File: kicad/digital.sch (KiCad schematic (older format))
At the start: 15 parts, among them P1 USART0, P3 ISP, P5 hole, P6 hole, P8 hole, P9 hole

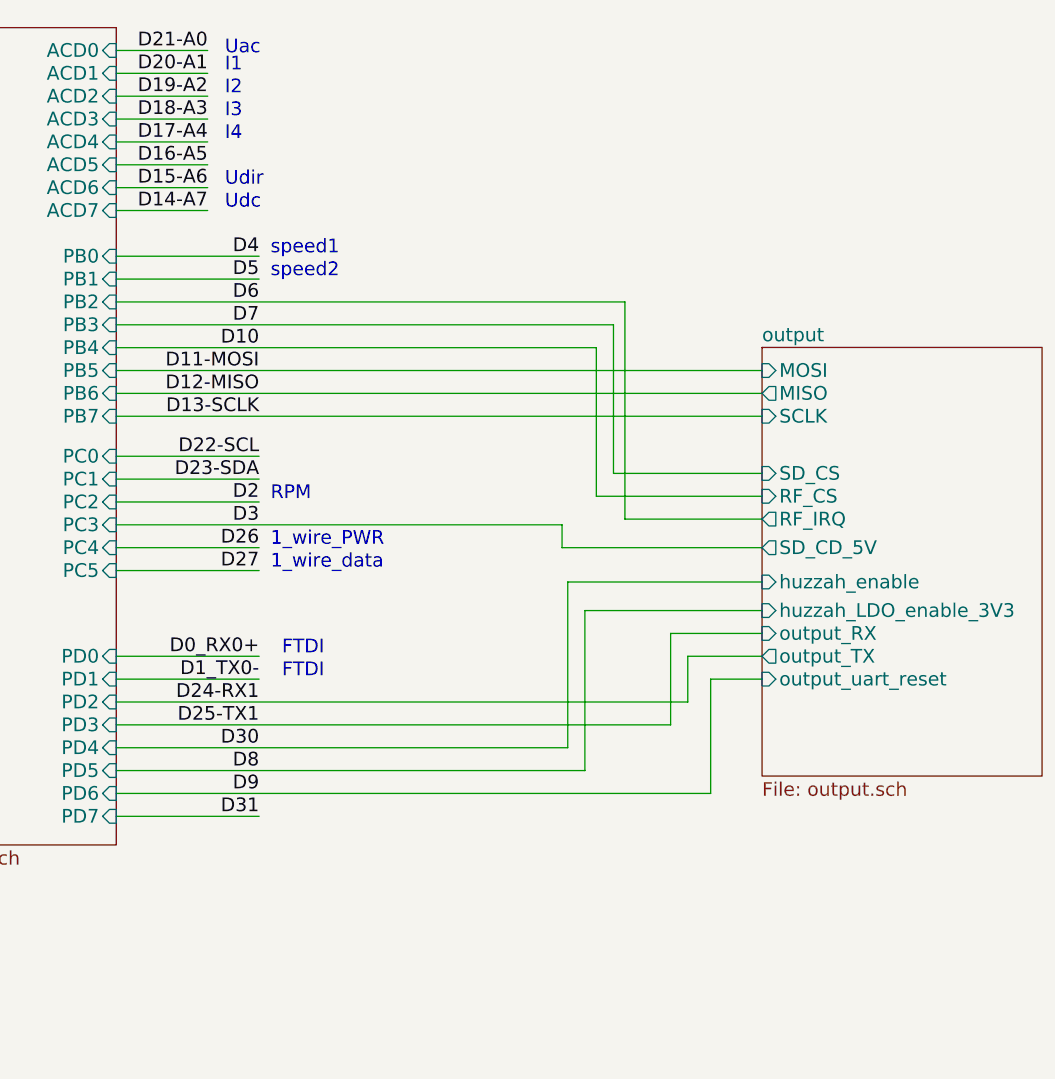
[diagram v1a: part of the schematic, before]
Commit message: add somes notes on schematics
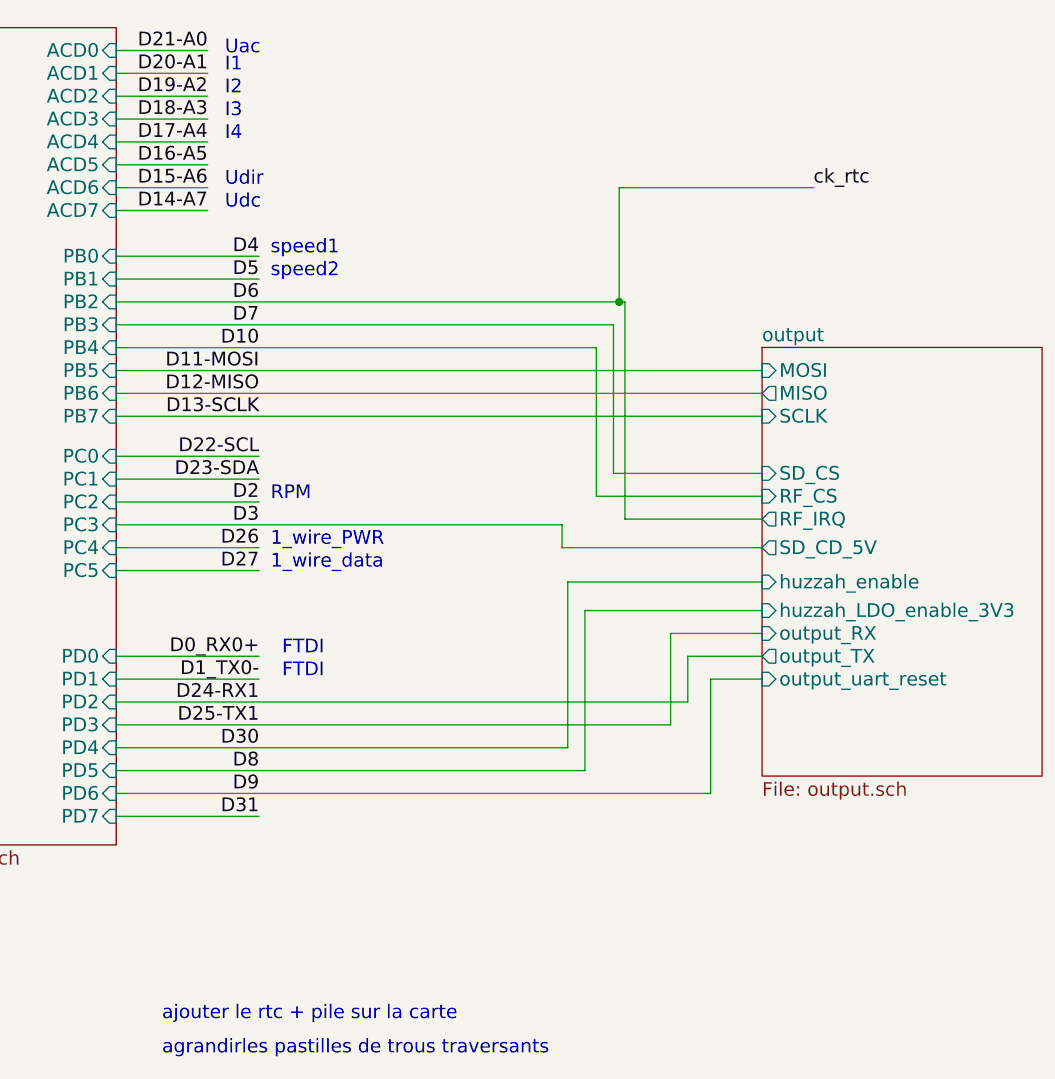
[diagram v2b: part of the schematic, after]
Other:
- note added: "agrandirles pastilles de trous traversants"
- note added: "ajouter le rtc + pile sur la carte"
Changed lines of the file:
@@
 Text Notes 9875 6175 0    60   ~ 0
 +5V\nGND\nTX0\nRX0\nDTR\n3V3
+Text Notes 2850 6400 0    60   ~ 0
+ajouter le rtc + pile sur la carte
+Text Notes 2850 6550 0    60   ~ 0
+agrandirles pastilles de trous traversants
+Wire Wire Line
+	4850 3250 4850 2750
+Wire Wire Line
+	4850 2750 5700 2750
+Connection ~ 4850 3250
+Text Label 5700 2750 0    60   ~ 0
+ck_rtc
 $EndSCHEMATC

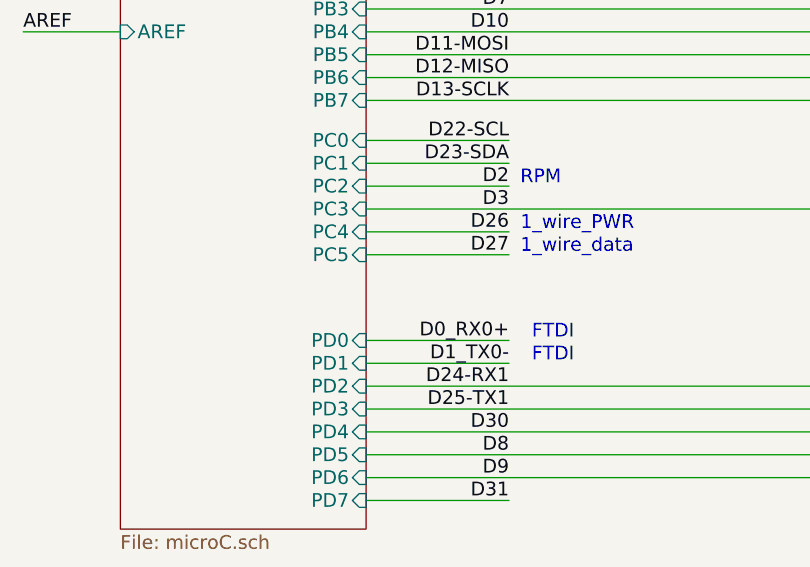
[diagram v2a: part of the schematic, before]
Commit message: Modify micro pins and unify ground in power supply
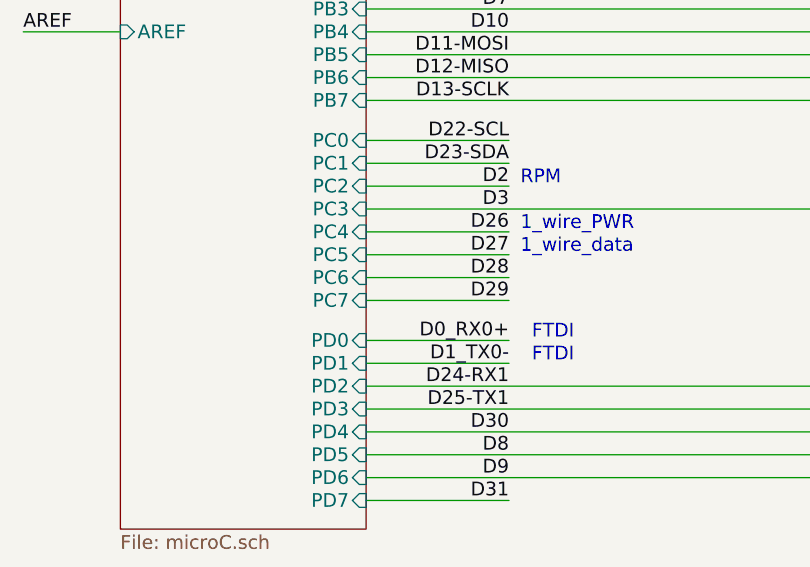
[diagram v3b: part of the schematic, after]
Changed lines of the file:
@@
 F32 "AREF" I L 1575 3450 60
 F33 "PC4" I R 2650 4325 60
+F34 "PC6" I R 2650 4525 60
+F35 "PC7" I R 2650 4625 60
 $EndSheet
 Text Label 3275 3550 2    60   ~ 0
@@
 Text Label 5700 2750 0    60   ~ 0
 ck_rtc
+Wire Wire Line
+	2650 4525 3275 4525
+Wire Wire Line
+	2650 4625 3275 4625
+Text Label 3275 4525 2    60   ~ 0
+D28
+Text Label 3275 4625 2    60   ~ 0
+D29
 $EndSCHEMATC
